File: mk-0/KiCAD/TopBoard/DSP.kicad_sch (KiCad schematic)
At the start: 75 parts, among them J1 Conn_01x04, J2 Conn_01x04, J4 Conn_01x15, U5 W25Q16JVSS, U8 ZL38063, Y1 12MHz

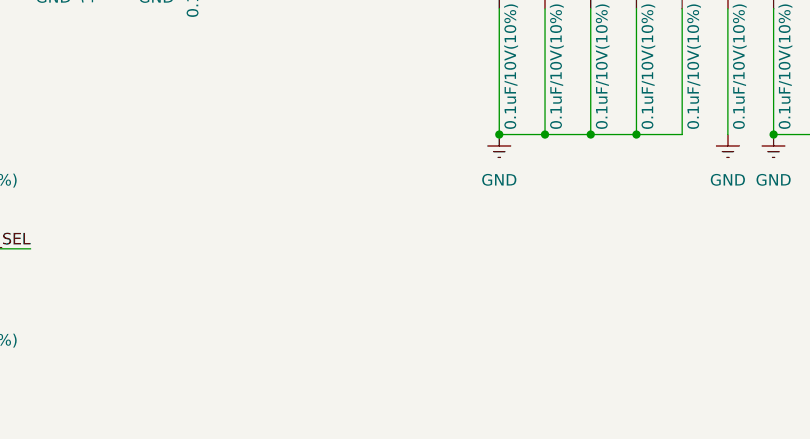
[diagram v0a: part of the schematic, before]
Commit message: Full routed and DRC completed
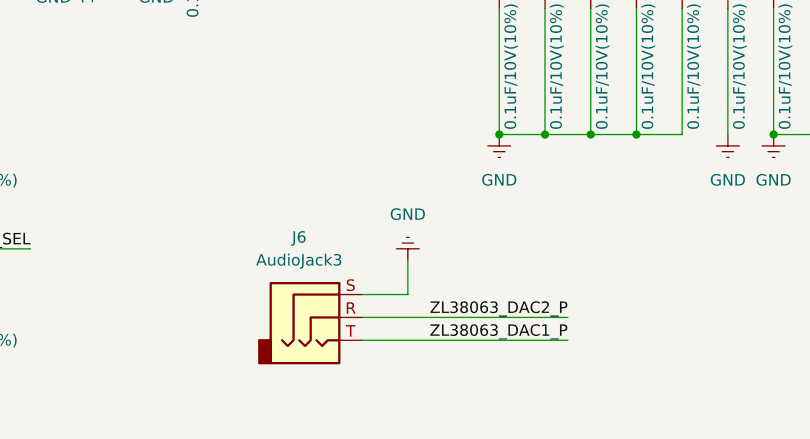
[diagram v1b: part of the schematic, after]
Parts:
- added J6: AudioJack3, Connector_Audio:Jack_3.5mm_CUI_SJ1-3533NG_Horizontal, symbol Connector_Audio:AudioJack3
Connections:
- net GND: now also J6.S
- net ZL38063_DAC1_P: now also J6.T
- net ZL38063_DAC2_P: now also J6.R
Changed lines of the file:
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@@
 	(wire
 		(pts
+			(xy 133.35 176.53) (xy 138.43 176.53)
+		)
+		(stroke
+			(width 0)
+			(type default)
+		)
+	)
+	(wire
+		(pts
 			(xy 217.17 102.87) (xy 246.38 102.87)
 		)
@@
 	(wire
 		(pts
+			(xy 133.35 181.61) (xy 156.21 181.61)
+		)
+		(stroke
+			(width 0)
+			(type default)
+		)
+	)
+	(wire
+		(pts
 			(xy 184.15 134.62) (xy 189.23 134.62)
 		)
@@
 	(wire
 		(pts
+			(xy 156.21 179.07) (xy 133.35 179.07)
+		)
+		(stroke
+			(width 0)
+			(type default)
+		)
+	)
+	(wire
+		(pts
 			(xy 168.91 134.62) (xy 168.91 137.16)
 		)
@@
 	(wire
 		(pts
+			(xy 138.43 176.53) (xy 138.43 172.72)
+		)
+		(stroke
+			(width 0)
+			(type default)
+		)
+	)
+	(wire
+		(pts
 			(xy 209.55 81.28) (xy 257.81 81.28)
 		)
@@
 		)
 	)
+	(label "ZL38063_DAC2_P"
+		(at 156.21 179.07 180)
+		(fields_autoplaced yes)
+		(effects
+			(font
+				(size 1.27 1.27)
+			)
+			(justify right bottom)
+		)
+	)
 	(label "EXT_SEL"
 		(at 96.52 171.45 180)
@@
 		)
 	)
+	(label "ZL38063_DAC1_P"
+		(at 156.21 181.61 180)
+		(fields_autoplaced yes)
+		(effects
+			(font
+				(size 1.27 1.27)
+			)
+			(justify right bottom)
+		)
+	)
 	(label "GPIO0"
 		(at 251.46 53.34 0)
@@
 	)
 	(symbol
+		(lib_id "power:Earth")
+		(at 138.43 172.72 180)
+		(unit 1)
+		(exclude_from_sim no)
+		(in_bom yes)
+		(on_board yes)
+		(dnp no)
+		(fields_autoplaced yes)
+		(property "Reference" "#PWR035"
+			(at 138.43 166.37 0)
+			(effects
+				(font
+					(size 1.27 1.27)
+				)
+				(hide yes)
+			)
+		)
+		(property "Value" "GND"
+			(at 138.43 167.64 0)
+			(effects
+				(font
+					(size 1.27 1.27)
+				)
+			)
+		)
+		(property "Footprint" ""
+			(at 138.43 172.72 0)
+			(effects
+				(font
+					(size 1.27 1.27)
+				)
+				(hide yes)
+			)
+		)
+		(property "Datasheet" "~"
+			(at 138.43 172.72 0)
+			(effects
+				(font
+					(size 1.27 1.27)
+				)
+				(hide yes)
+			)
+		)
+		(property "Description" "Power symbol creates a global label with name \"Earth\""
+			(at 138.43 172.72 0)
+			(effects
+				(font
+					(size 1.27 1.27)
+				)
+				(hide yes)
+			)
+		)
+		(pin "1"
+		)
+		(instances
+			(project "TopBoard"
+				(path "/e63e39d7-6ac0-4ffd-8aa3-1841a4541b55/958c7b0d-baa0-4852-b175-63ea9119e9f3"
+					(reference "#PWR035")
+					(unit 1)
+				)
+			)
+		)
+	)
+	(symbol
 		(lib_id "Device:R")
 		(at 129.54 50.8 90)
@@
 					(unit 1)
 				)
+			)
+		)
+	)
+	(symbol
+		(lib_id "Connector_Audio:AudioJack3")
+		(at 128.27 179.07 0)
+		(unit 1)
+		(exclude_from_sim no)
+		(in_bom yes)
+		(on_board yes)
+		(dnp no)
+		(fields_autoplaced yes)
+		(property "Reference" "J6"
+			(at 126.365 170.18 0)
+			(effects
+				(font
+					(size 1.27 1.27)
+				)
+			)
+		)
+		(property "Value" "AudioJack3"
+			(at 126.365 172.72 0)
+			(effects
+				(font
+					(size 1.27 1.27)
+				)
+			)
+		)
+		(property "Footprint" "Connector_Audio:Jack_3.5mm_CUI_SJ1-3533NG_Horizontal"
+			(at 128.27 179.07 0)
+			(effects
+				(font
+					(size 1.27 1.27)
+				)
+				(hide yes)
+			)
+		)
+		(property "Datasheet" "~"
+			(at 128.27 179.07 0)
+			(effects
+				(font
+					(size 1.27 1.27)
+				)
+				(hide yes)
+			)
+		)
+		(property "Description" "Audio Jack, 3 Poles (Stereo / TRS)"
+			(at 128.27 179.07 0)
+			(effects
+				(font
+					(size 1.27 1.27)
+				)
+				(hide yes)
+			)
+		)
+		(pin "R"
+		)
+		(pin "T"
+		)
+		(pin "S"
+		)
+		(instances
+			(project "TopBoard"
+				(path "/e63e39d7-6ac0-4ffd-8aa3-1841a4541b55/958c7b0d-baa0-4852-b175-63ea9119e9f3"
+					(reference "J6")
+					(unit 1)
+				)

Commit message: Cleanup and naming of Touchpoints
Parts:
- J6: now not fitted; now left out of the parts list
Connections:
- net +3V3: now also J1.4 (Pin_4)
- net GND: now also J1.1 (Pin_1); no longer J1.4 (Pin_4)
- net ZL38063_UART_RX: now also J1.3 (Pin_3); no longer J1.2 (Pin_2)
- net ZL38063_UART_TX: now also J1.2 (Pin_2); no longer J1.3 (Pin_3)
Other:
- note added: "Bootstrap"
- moved on the sheet: C1, C11, C12, C13, C14, C15, C16, C17, C18, C19, C20, C21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

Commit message: Silkscreen text alignment
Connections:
- net +3V3: now also J4.15 (Pin_15); no longer J4.1 (Pin_1)
- net GND: now also J4.1 (Pin_1); no longer J4.15 (Pin_15)
- net GPIO0: now also J4.14 (Pin_14); no longer J4.2 (Pin_2)
- net GPIO1: now also J4.13 (Pin_13); no longer J4.3 (Pin_3)
- net GPIO2: now also J4.12 (Pin_12); no longer J4.4 (Pin_4)
- net at U8.37 (GPIO_3): now also J4.11 (Pin_11); no longer J4.5 (Pin_5)
- net at U8.38 (GPIO_4): now also J4.10 (Pin_10); no longer J4.6 (Pin_6)
- net at U8.39 (GPIO_5): now also J4.9 (Pin_9); no longer J4.7 (Pin_7)
- net at U8.41 (GPIO_7): now also J4.7 (Pin_7); no longer J4.9 (Pin_9)
- net at U8.43 (GPIO_8): now also J4.6 (Pin_6); no longer J4.10 (Pin_10)
- net at U8.44 (GPIO_10): now also J4.5 (Pin_5); no longer J4.11 (Pin_11)
- net at U8.45 (GPIO_11): now also J4.4 (Pin_4); no longer J4.12 (Pin_12)
- net at U8.47 (GPIO_12): now also J4.3 (Pin_3); no longer J4.13 (Pin_13)
- net at U8.48 (GPIO_13): now also J4.2 (Pin_2); no longer J4.14 (Pin_14)
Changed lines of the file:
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@@
 	)
 	(symbol
-		(lib_id "Connector_Generic:Conn_01x15")
-		(at 260.35 68.58 0)
-		(unit 1)
-		(exclude_from_sim no)
-		(in_bom no)
-		(on_board yes)
-		(dnp yes)
-		(fields_autoplaced yes)
-		(property "Reference" "J4"
-			(at 262.89 67.3099 0)
-			(effects
-				(font
-					(size 1.27 1.27)
-				)
-				(justify left)
-			)
-		)
-		(property "Value" "Conn_01x15"
-			(at 262.89 69.8499 0)
-			(effects
-				(font
-					(size 1.27 1.27)
-				)
-				(justify left)
-			)
-		)
-		(property "Footprint" "Connector_PinHeader_2.54mm:PinHeader_1x15_P2.54mm_Vertical"
-			(at 260.35 68.58 0)
-			(effects
-				(font
-					(size 1.27 1.27)
-				)
-				(hide yes)
-			)
-		)
-		(property "Datasheet" "~"
-			(at 260.35 68.58 0)
-			(effects
-				(font
-					(size 1.27 1.27)
-				)
-				(hide yes)
-			)
-		)
-		(property "Description" "Generic connector, single row, 01x15, script generated (kicad-library-utils/schlib/autogen/connector/)"
-			(at 260.35 68.58 0)
-			(effects
-				(font
-					(size 1.27 1.27)
-				)
-				(hide yes)
-			)
-		)
-		(pin "3"
-		)
-		(pin "8"
-		)
-		(pin "14"
-		)
-		(pin "4"
-		)
-		(pin "10"
-		)
-		(pin "13"
-		)
-		(pin "12"
-		)
-		(pin "11"
-		)
-		(pin "1"
-		)
-		(pin "15"
-		)
-		(pin "6"
-		)
-		(pin "5"
-		)
-		(pin "7"
-		)
-		(pin "9"
-		)
-		(pin "2"
-		)
-		(instances
-			(project "TopBoard"
-				(path "/e63e39d7-6ac0-4ffd-8aa3-1841a4541b55/958c7b0d-baa0-4852-b175-63ea9119e9f3"
-					(reference "J4")
-					(unit 1)
-				)
-			)
-		)
-	)
-	(symbol
 		(lib_id "Jumper:SolderJumper_3_Open")
 		(at 43.18 153.67 90)
@@
 					(unit 1)
 				)
+			)
+		)
+	)
+	(symbol
+		(lib_id "Connector_Generic:Conn_01x15")
+		(at 260.35 68.58 0)
+		(mirror x)
+		(unit 1)
+		(exclude_from_sim no)
+		(in_bom no)
+		(on_board yes)
+		(dnp yes)
+		(property "Reference" "J4"
+			(at 262.89 69.8501 0)
+			(effects
+				(font
+					(size 1.27 1.27)
+				)
+				(justify left)
+			)
+		)
+		(property "Value" "Conn_01x15"
+			(at 262.89 67.3101 0)
+			(effects
+				(font
+					(size 1.27 1.27)
+				)
+				(justify left)
+			)
+		)
+		(property "Footprint" "Connector_PinHeader_2.54mm:PinHeader_1x15_P2.54mm_Vertical"
+			(at 260.35 68.58 0)
+			(effects
+				(font
+					(size 1.27 1.27)
+				)
+				(hide yes)
+			)
+		)
+		(property "Datasheet" "~"
+			(at 260.35 68.58 0)
+			(effects
+				(font
+					(size 1.27 1.27)
+				)
+				(hide yes)
+			)
+		)
+		(property "Description" "Generic connector, single row, 01x15, script generated (kicad-library-utils/schlib/autogen/connector/)"
+			(at 260.35 68.58 0)
+			(effects
+				(font
+					(size 1.27 1.27)
+				)
+				(hide yes)
+			)
+		)
+		(pin "3"
+		)
+		(pin "8"
+		)
+		(pin "14"
+		)
+		(pin "4"
+		)
+		(pin "10"
+		)
+		(pin "13"
+		)
+		(pin "12"
+		)
+		(pin "11"
+		)
+		(pin "1"
+		)
+		(pin "15"
+		)
+		(pin "6"
+		)
+		(pin "5"
+		)
+		(pin "7"
+		)
+		(pin "9"
+		)
+		(pin "2"
+		)
+		(instances
+			(project "TopBoard"
+				(path "/e63e39d7-6ac0-4ffd-8aa3-1841a4541b55/958c7b0d-baa0-4852-b175-63ea9119e9f3"
+					(reference "J4")
+					(unit 1)
+				)
